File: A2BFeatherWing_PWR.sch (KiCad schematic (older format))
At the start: 2 parts

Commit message: added datasheets, power
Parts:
- added C?: 47p, symbol Device:C_Small
- added C?: 22u, symbol Device:C_Small
- added C?: C_Small, symbol Device:C_Small
- added D?: MBR0520, Diode_SMD:D_SOD-123, symbol Diode:MBR0520
- added R?: 60k4, symbol Device:R_Small
- added R?: 11k3, symbol Device:R_Small
- U?: symbol Knochi_Analog:LT1930 -> A2BFeatherWing-rescue:LT1930-Knochi_Analog
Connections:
- net at U?.1 (SW): now also L?.2, D?.2 (A)
- net GND: now reaches U?.2 (GND)
- net GND: now also C?.2, C?.2, R?.2
- net at U?.3 (FB): now also C?.2, R?.1, R?.2
- net EN: now reaches U?.4 (~SHDN)
- net at U?.5 (VIN): now also L?.1, C?.1
- new net: C?.1, C?.1, D?.1 (K), R?.1
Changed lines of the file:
@@
 $EndDescr
 $Comp
-L Knochi_Analog:LT1930 U?
+L A2BFeatherWing-rescue:LT1930-Knochi_Analog U?
 U 1 1 5DC5E4DB
 P 4900 3400
@@
 	0    -1   -1   0
 $EndComp
-Text Notes 3100 3450 0    50   ~ 0
+Text Notes 3350 2225 0    50   ~ 0
 DC= 9V-3.8V/9V=  57.8%
 $Bitmap
-Pos 6600 2950
+Pos 7575 2875
 Scale 1.000000
 Data
@@
 EndData
 $EndBitmap
+$Comp
+L Device:R_Small R?
+U 1 1 5E1530AD
+P 5525 3450
+F 0 "R?" H 5584 3496 50  0000 L CNN
+F 1 "60k4" H 5584 3405 50  0000 L CNN
+F 2 "" H 5525 3450 50  0001 C CNN
+F 3 "~" H 5525 3450 50  0001 C CNN
+	1    5525 3450
+	1    0    0    -1
+$EndComp
+$Comp
+L Device:R_Small R?
+U 1 1 5E153E0F
+P 5525 3825
+F 0 "R?" H 5584 3871 50  0000 L CNN
+F 1 "11k3" H 5584 3780 50  0000 L CNN
+F 2 "" H 5525 3825 50  0001 C CNN
+F 3 "~" H 5525 3825 50  0001 C CNN
+	1    5525 3825
+	1    0    0    -1
+$EndComp
+$Comp
+L Device:C_Small C?
+U 1 1 5E1542E9
+P 5850 3450
+F 0 "C?" H 5942 3496 50  0000 L CNN
+F 1 "47p" H 5942 3405 50  0000 L CNN
+F 2 "" H 5850 3450 50  0001 C CNN
+F 3 "~" H 5850 3450 50  0001 C CNN
+	1    5850 3450
+	1    0    0    -1
+$EndComp
+$Comp
+L Device:C_Small C?
+U 1 1 5E154E93
+P 6175 3650
+F 0 "C?" H 6267 3696 50  0000 L CNN
+F 1 "22u" H 6267 3605 50  0000 L CNN
+F 2 "" H 6175 3650 50  0001 C CNN
+F 3 "~" H 6175 3650 50  0001 C CNN
+	1    6175 3650
+	1    0    0    -1
+$EndComp
+$Comp
+L Diode:MBR0520 D?
+U 1 1 5E15545F
+P 5275 3250
+F 0 "D?" H 5275 3034 50  0000 C CNN
+F 1 "MBR0520" H 5275 3125 50  0000 C CNN
+F 2 "Diode_SMD:D_SOD-123" H 5275 3075 50  0001 C CNN
+F 3 "http://www.mccsemi.com/up_pdf/MBR0520~MBR0580(SOD123).pdf" H 5275 3250 50  0001 C CNN
+	1    5275 3250
+	-1   0    0    1
+$EndComp
+$Comp
+L Device:C_Small C?
+U 1 1 5E157240
+P 4050 3500
+F 0 "C?" H 4142 3546 50  0000 L CNN
+F 1 "C_Small" H 4142 3455 50  0000 L CNN
+F 2 "" H 4050 3500 50  0001 C CNN
+F 3 "~" H 4050 3500 50  0001 C CNN
+	1    4050 3500
+	1    0    0    -1
+$EndComp
+Wire Wire Line
+	5300 3650 5525 3650
+Wire Wire Line
+	5525 3650 5525 3550
+Wire Wire Line
+	5525 3725 5525 3650
+Connection ~ 5525 3650
+$Comp
+L power:GND #PWR?
+U 1 1 5E158970
+P 5525 4125
+F 0 "#PWR?" H 5525 3875 50  0001 C CNN
+F 1 "GND" H 5530 3952 50  0000 C CNN
+F 2 "" H 5525 4125 50  0001 C CNN
+F 3 "" H 5525 4125 50  0001 C CNN
+	1    5525 4125
+	1    0    0    -1
+$EndComp
+Wire Wire Line
+	5425 3250 5525 3250
+Wire Wire Line
+	5525 3250 5525 3350
+Wire Wire Line
+	5850 3350 5850 3250
+Wire Wire Line
+	5850 3250 5525 3250
+Connection ~ 5525 3250
+Wire Wire Line
+	5850 3250 6175 3250
+Wire Wire Line
+	6175 3250 6175 3550
+Connection ~ 5850 3250
+Wire Wire Line
+	5850 3550 5850 3650
+Wire Wire Line
+	5850 3650 5525 3650
+Wire Wire Line
+	5525 3925 5525 4125
+$Comp
+L power:GND #PWR?
+U 1 1 5E159EDA
+P 6175 4125
+F 0 "#PWR?" H 6175 3875 50  0001 C CNN
+F 1 "GND" H 6180 3952 50  0000 C CNN
+F 2 "" H 6175 4125 50  0001 C CNN
+F 3 "" H 6175 4125 50  0001 C CNN
+	1    6175 4125
+	1    0    0    -1
+$EndComp
+Wire Wire Line
+	6175 4125 6175 3750
+$Comp
+L power:GND #PWR?
+U 1 1 5E15A4F3
+P 4900 4125
+F 0 "#PWR?" H 4900 3875 50  0001 C CNN
+F 1 "GND" H 4905 3952 50  0000 C CNN
+F 2 "" H 4900 4125 50  0001 C CNN
+F 3 "" H 4900 4125 50  0001 C CNN
+	1    4900 4125
+	1    0    0    -1
+$EndComp
+Wire Wire Line
+	4900 4125 4900 3950
+Wire Wire Line
+	5050 3300 5050 3250
+Wire Wire Line
+	5050 3250 5125 3250
+Wire Wire Line
+	5000 3250 5050 3250
+Connection ~ 5050 3250
+Wire Wire Line
+	4800 3250 4750 3250
+Wire Wire Line
+	4750 3250 4750 3300
+Wire Wire Line
+	4750 3250 4050 3250
+Wire Wire Line
+	4050 3250 4050 3400
+$Comp
+L power:GND #PWR?
+U 1 1 5E15B821
+P 4050 4125
+F 0 "#PWR?" H 4050 3875 50  0001 C CNN
+F 1 "GND" H 4055 3952 50  0000 C CNN
+F 2 "" H 4050 4125 50  0001 C CNN
+F 3 "" H 4050 4125 50  0001 C CNN
+	1    4050 4125
+	1    0    0    -1
+$EndComp
+Wire Wire Line
+	4050 3600 4050 4125
+Connection ~ 4750 3250
+Text HLabel 4350 3650 0    50   Input ~ 0
+EN
+Wire Wire Line
+	4350 3650 4500 3650
+$Comp
+L power:+BATT #PWR?
+U 1 1 5E15CE4C
+P 1825 2950
+F 0 "#PWR?" H 1825 2800 50  0001 C CNN
+F 1 "+BATT" H 1840 3123 50  0000 C CNN
+F 2 "" H 1825 2950 50  0001 C CNN
+F 3 "" H 1825 2950 50  0001 C CNN
+	1    1825 2950
+	1    0    0    -1
+$EndComp
+$Comp
+L A2BFeatherWing:VUSB #PWR?
+U 1 1 5E15E9F8
+P 2275 2950
+F 0 "#PWR?" H 2275 2800 50  0001 C CNN
+F 1 "VUSB" H 2290 3123 50  0000 C CNN
+F 2 "" H 2275 2950 50  0001 C CNN
+F 3 "" H 2275 2950 50  0001 C CNN
+	1    2275 2950
+	1    0    0    -1
+$EndComp
 $EndSCHEMATC

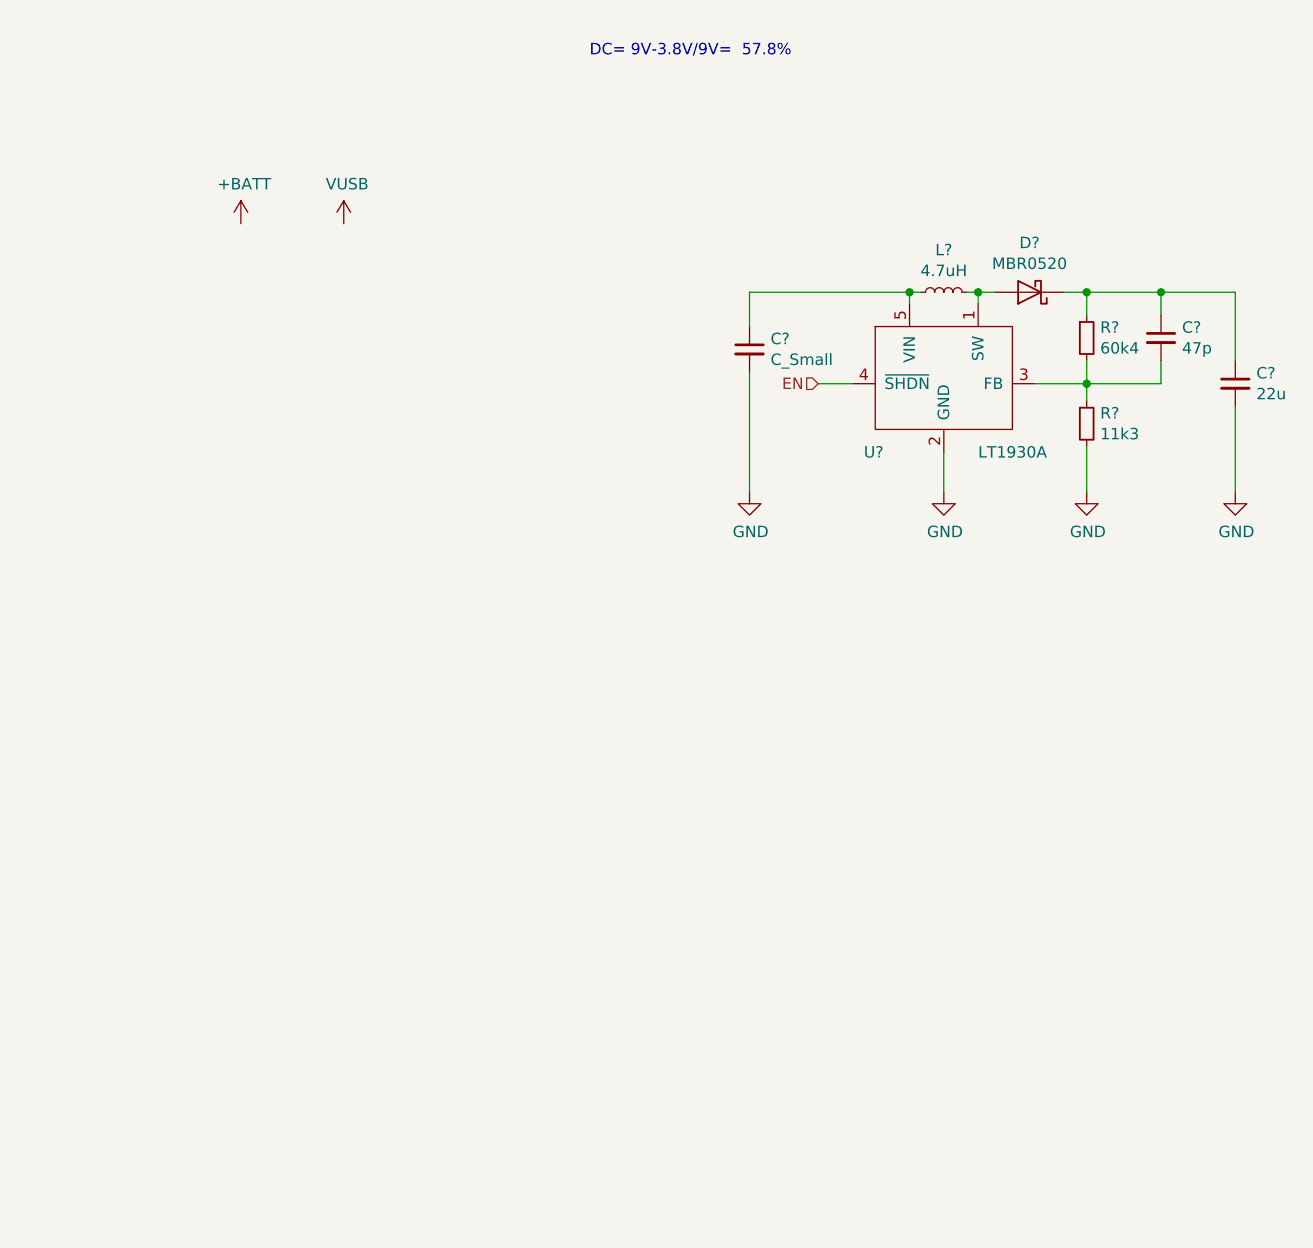
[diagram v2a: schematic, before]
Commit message: added 3d model of JST PH and CM added eco layer for silkscreen
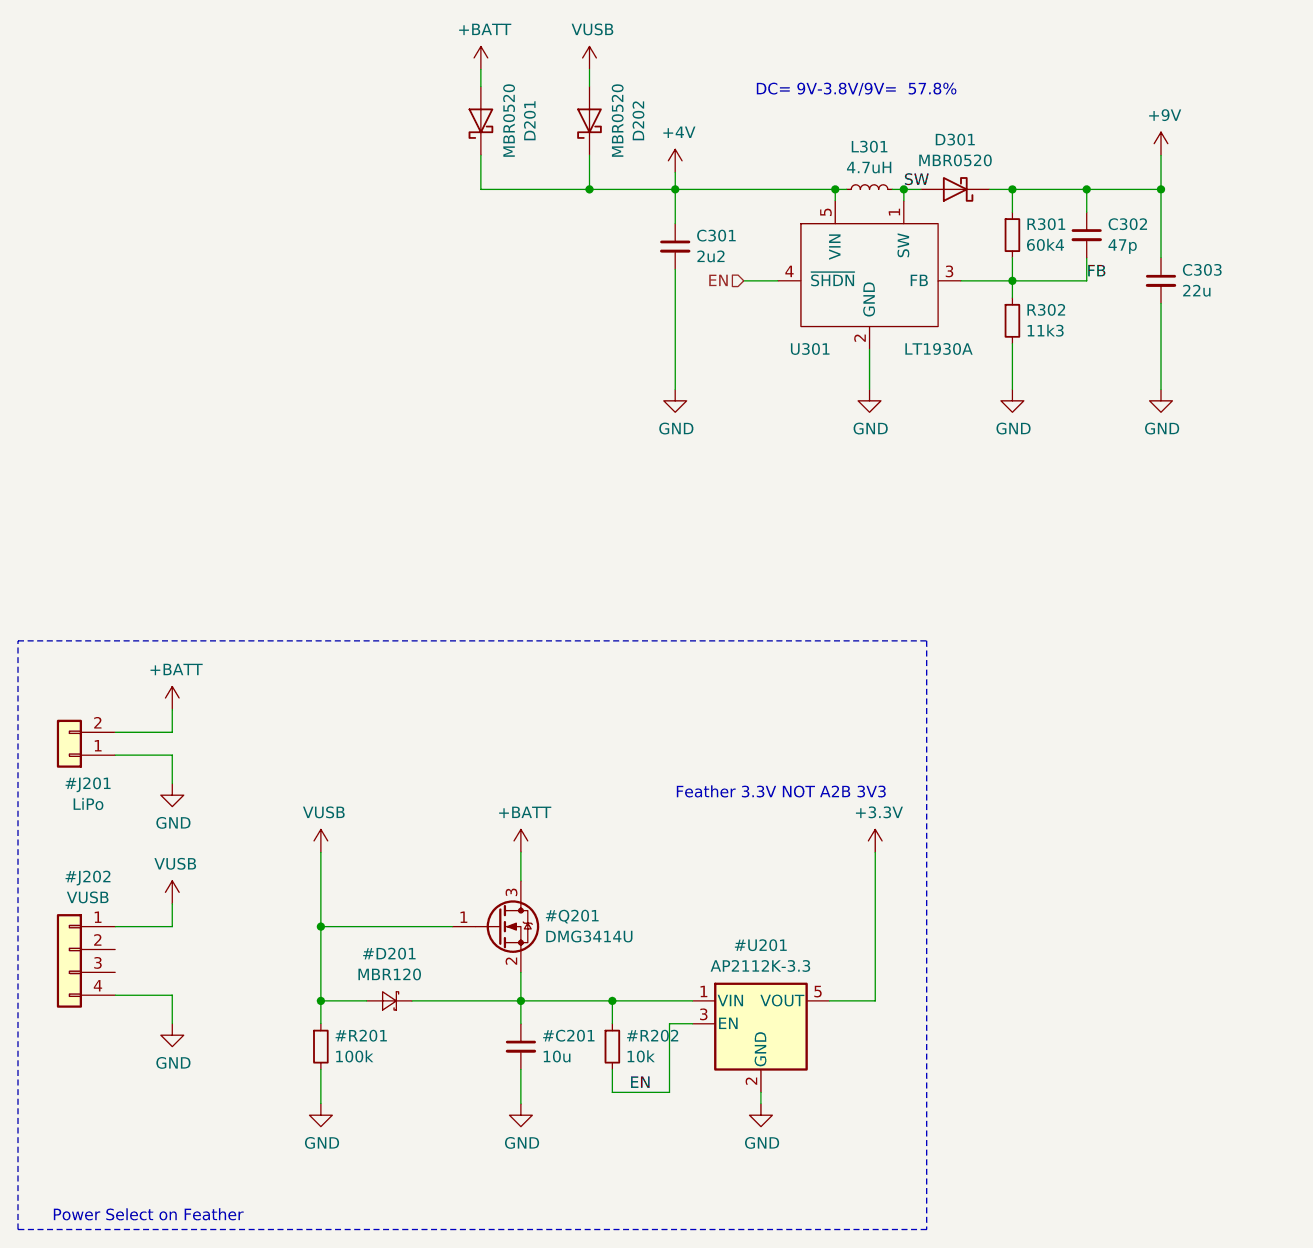
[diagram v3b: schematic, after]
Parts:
- added D201, D202: MBR0520, Diode_SMD:D_SOD-123, symbol Diode:MBR0520
- C301: renamed from C?; value C_Small -> 2u2; footprint (none) -> Capacitor_SMD:C_0805_2012Metric
- C302: renamed from C?; footprint (none) -> Capacitor_SMD:C_0402_1005Metric
- C303: renamed from C?; footprint (none) -> Capacitor_SMD:C_1812_4532Metric
- L301: renamed from L?; footprint (none) -> A2BFeatherWing:L_Sumida_CR43_4.3x4.8x3.5mm; DK_Datasheet_Link https://media.digikey.com/pdf/Data%20Sheets/Murata%20PDFs/L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 -> (none); MPN LQH32PN4R7NN0L -> CR43NP-4R7MC; Manufacturer Murata -> Sumida
- R301, R302: renamed from R?; footprint (none) -> Resistor_SMD:R_0402_1005Metric
- U301: renamed from U?; footprint (none) -> Package_TO_SOT_SMD:SOT-23-5
- gave numbers to parts that had none: 1
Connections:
- net +BATT: now also D201.2 (A)
- net VUSB: now also D202.2 (A)
- net SW: now reaches D301.2 (A), L301.2, U301.1 (SW)
- net FB: now reaches C302.2, R301.2, R302.1, U301.3 (FB)
- net +4V: now reaches C301.1, L301.1, U301.5 (VIN)
- net +4V: now also D201.1 (K), D202.1 (K)
- net +9V: now reaches C302.1, C303.1, D301.1 (K), R301.1
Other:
- note added: "Feather 3.3V NOT A2B 3V3"
- note added: "Power Select on Feather"
- moved on the sheet: C301, C302, C303, D301, L301, R301, R302, U301

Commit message: last changes
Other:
- note added: "Power Select on Feather (not on this PCB)\n"
- note removed: "Power Select on Feather"
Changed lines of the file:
@@
 	850  4775 4825 4775
 Wire Notes Line
-	4825 4775 4825 7350
+	4825 4775 4825 7100
 Wire Notes Line
-	4825 7350 850  7350
+	4825 7100 850  7100
 Wire Notes Line
-	850  7350 850  4775
-Text Notes 1000 7325 0    50   ~ 0
-Power Select on Feather
+	850  7100 850  4775
+Text Notes 850  7200 0    50   ~ 0
+Power Select on Feather (not on this PCB)\n
 Wire Wire Line
 	3350 2275 3350 2350
